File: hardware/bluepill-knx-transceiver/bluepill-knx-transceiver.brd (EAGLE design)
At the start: 37.6 x 38 mm, 22 parts, among them T1 BC856, T2 IRLL110

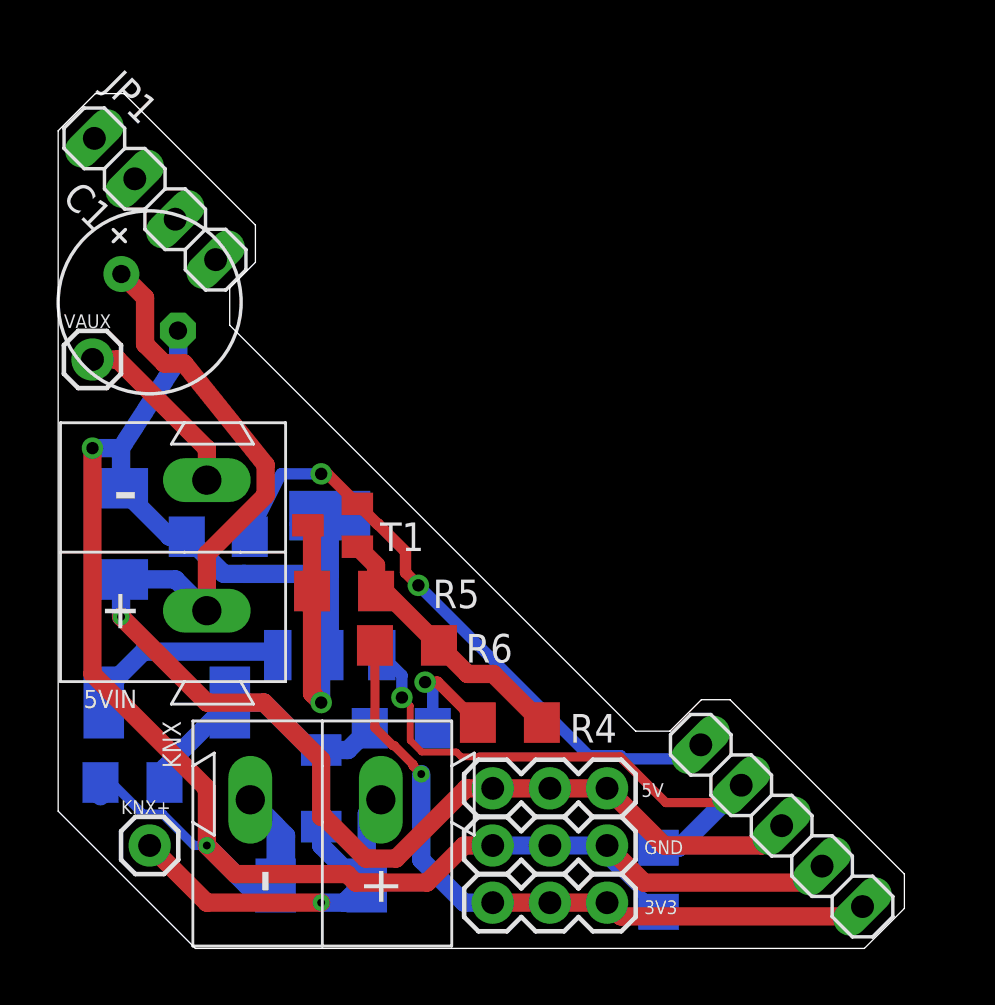
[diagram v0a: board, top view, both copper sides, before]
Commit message: transceiver board GND fills
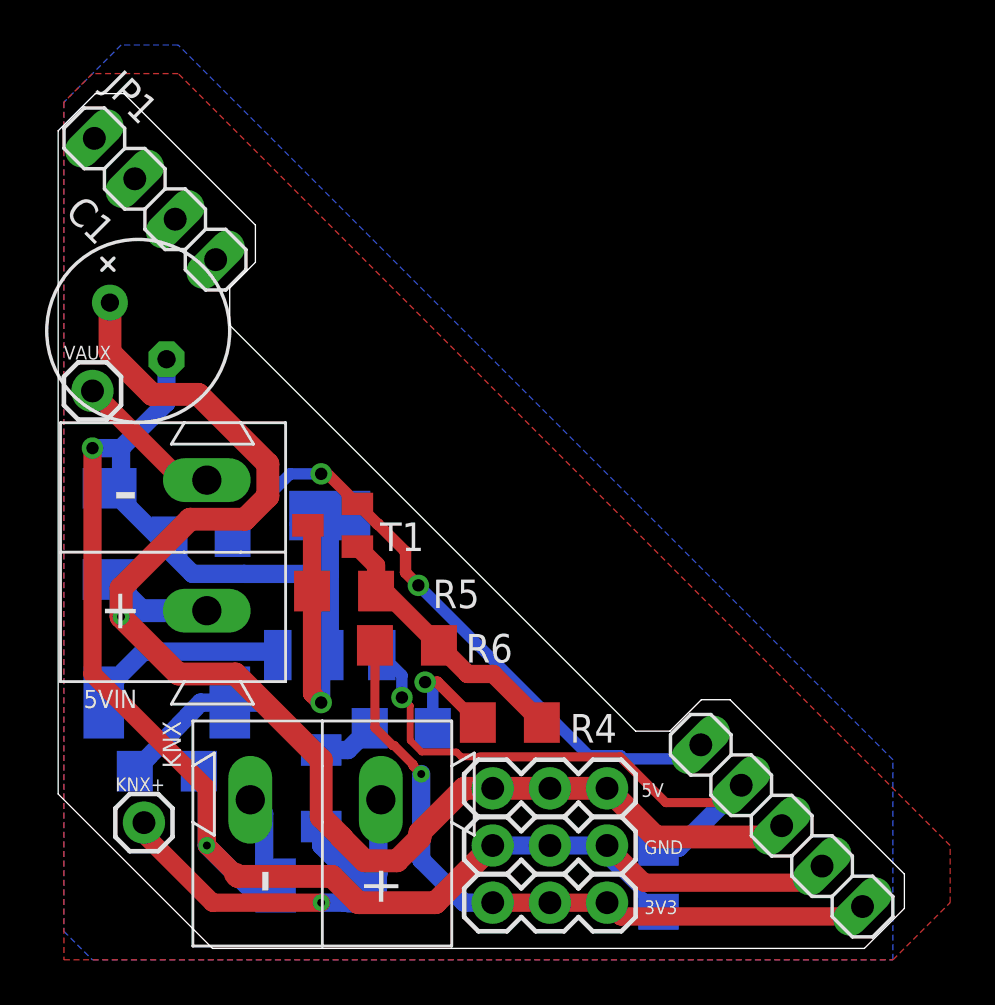
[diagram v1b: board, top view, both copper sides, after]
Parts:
- moved R3 1.61 mm to (60.5, 27.4), turned to 0 degrees
- moved VAUX 1.40 mm to (57.1, 44.3)
- moved C1 1.37 mm to (59.2, 47.0)
- moved KNX+ 1.05 mm to (59.4, 25.1)
- moved C3 0.76 mm to (62.0, 37.8)
- moved D1 0.51 mm to (57.9, 38.0)
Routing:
- net GND: track 111.8 -> 104.2 mm
- net 5V: track 63.0 -> 66.9 mm
- net VAUX: track 8.12 -> 6.72 mm
- net EIB+: track 19.1 -> 19.9 mm
- net KNX+D: track 12.2 -> 13.0 mm
- added copper zone on layer 1, net GND
- added copper zone on layer 16, net GND
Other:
- outline, holes or cut-outs redrawn

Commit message: prepared for DCDC
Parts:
- added CSEL: (no value), jumper:SJ_2
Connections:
- new net N$3: C1.+, CSEL.2
- net 5V: now also CSEL.1; no longer C1.+
- net VAUX: now also CSEL.3
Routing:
- net N$3: track 0.00 -> 8.71 mm
- net GND: track 104.2 -> 111.9 mm
- net 5V: track 66.9 -> 60.5 mm, vias 1 -> 2
- net VAUX: track 6.72 -> 7.70 mm
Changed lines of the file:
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@@
 <layer number="27" name="tValues" color="7" fill="1" visible="no" active="yes"/>
 <layer number="28" name="bValues" color="7" fill="1" visible="no" active="yes"/>
-<layer number="29" name="tStop" color="7" fill="3" visible="no" active="yes"/>
+<layer number="29" name="tStop" color="7" fill="3" visible="yes" active="yes"/>
 <layer number="30" name="bStop" color="7" fill="6" visible="no" active="yes"/>
 <layer number="31" name="tCream" color="7" fill="4" visible="no" active="yes"/>
@@
 <wire x1="58.547" y1="57.531" x2="57.277" y2="57.531" width="0" layer="20"/>
 <wire x1="55.626" y1="55.88" x2="57.277" y2="57.531" width="0" layer="20"/>
+<rectangle x1="59.69" y1="36.576" x2="65.151" y2="37.719" layer="29"/>
 </plain>
 <attributes>
@@
 <attribute name="VALUE" x="73.66" y="19.558" size="0.6096" layer="27" font="vector" ratio="20"/>
 </element>
+<element name="CSEL" library="jumper" library_urn="urn:adsk.eagle:library:252" package="SJ_2" package3d_urn="urn:adsk.eagle:package:15474/1" value="" x="62.738" y="43.053" rot="MR0"/>
 </elements>
 <signals>
@@
 <wire x1="64.777" y1="22.86" x2="65.285" y2="22.352" width="0.8128" layer="16"/>
 <wire x1="66.718" y1="38.354" x2="66.904" y2="38.168" width="0.8128" layer="1"/>
-<wire x1="66.904" y1="38.168" x2="66.904" y2="35.433" width="0.8128" layer="1"/>
+<wire x1="66.904" y1="38.168" x2="66.904" y2="36.83" width="0.8128" layer="1"/>
+<wire x1="66.904" y1="36.83" x2="66.904" y2="35.433" width="0.8128" layer="1"/>
 <wire x1="66.904" y1="35.433" x2="66.904" y2="30.886" width="0.8128" layer="1"/>
 <wire x1="66.904" y1="30.886" x2="67.31" y2="30.48" width="0.8128" layer="1"/>
@@
 <wire x1="63.88240625" y1="36.1964" x2="63.88380625" y2="36.195" width="0.8128" layer="16"/>
 <wire x1="63.88380625" y1="36.195" x2="67.691" y2="36.195" width="0.8128" layer="16"/>
-<wire x1="60.439234375" y1="43.802234375" x2="60.439234375" y2="45.7327625" width="0.8128" layer="16"/>
-<wire x1="58.42" y1="41.783" x2="60.439234375" y2="43.802234375" width="0.8128" layer="16"/>
 <wire x1="63.88240625" y1="36.1964" x2="61.5936" y2="36.1964" width="0.8128" layer="16"/>
 <wire x1="60.576" y1="37.214" x2="60.576" y2="37.846" width="0.8128" layer="16"/>
@@
 <wire x1="72.39" y1="21.59" x2="74.93" y2="24.13" width="1.016" layer="1"/>
 <wire x1="68.96236875" y1="21.59" x2="72.39" y2="21.59" width="1.016" layer="1"/>
+<wire x1="57.15" y1="41.783" x2="60.439234375" y2="45.072234375" width="1.016" layer="1"/>
+<wire x1="60.439234375" y1="45.072234375" x2="60.439234375" y2="45.7327625" width="1.016" layer="1"/>
+<wire x1="66.904" y1="36.83" x2="66.523" y2="37.211" width="1.016" layer="1"/>
+<wire x1="66.523" y1="37.211" x2="59.944" y2="37.211" width="1.016" layer="1"/>
 </signal>
 <signal name="PB8_KNX_RX">
@@
 <wire x1="70.89675625" y1="31.69384375" x2="70.0024" y2="32.5882" width="0.508" layer="16"/>
 <wire x1="74.3513375" y1="28.067" x2="80.5886625" y2="28.067" width="0.4064" layer="1"/>
-<wire x1="71.7776625" y1="28.2831" x2="73.3169" y2="28.2831" width="0.3048" layer="1"/>
 <wire x1="71.26506875" y1="30.33493125" x2="70.89675625" y2="30.70324375" width="0.3048" layer="1"/>
-<wire x1="71.7776625" y1="28.2831" x2="71.26506875" y2="28.79569375" width="0.3048" layer="1"/>
 <wire x1="71.26506875" y1="28.79569375" x2="71.26506875" y2="30.33493125" width="0.3048" layer="1"/>
-<wire x1="73.3169" y1="28.2831" x2="73.533" y2="28.067" width="0.3048" layer="1"/>
-<wire x1="73.533" y1="28.067" x2="74.3513375" y2="28.067" width="0.3048" layer="1"/>
+<wire x1="73.533" y1="28.067" x2="73.66" y2="28.067" width="0.3048" layer="1"/>
 <contactref element="JP1" pad="17"/>
+<wire x1="73.66" y1="28.067" x2="74.3513375" y2="28.067" width="0.3048" layer="1"/>
 <wire x1="85.197665625" y1="26.035" x2="85.96933125" y2="26.806665625" width="0.4064" layer="1"/>
 <wire x1="80.5886625" y1="28.067" x2="82.6206625" y2="26.035" width="0.4064" layer="1"/>
@@
 <wire x1="82.296" y1="24.028" x2="83.190665625" y2="24.028" width="0.8128" layer="16"/>
 <wire x1="83.190665625" y1="24.028" x2="85.96933125" y2="26.806665625" width="0.8128" layer="16"/>
+<wire x1="72.10259375" y1="28.067" x2="72.07999375" y2="28.0896" width="0.3048" layer="1"/>
+<wire x1="72.07999375" y1="28.0896" x2="71.9711625" y2="28.0896" width="0.3048" layer="1"/>
+<wire x1="73.533" y1="28.067" x2="72.10259375" y2="28.067" width="0.3048" layer="1"/>
+<wire x1="71.9711625" y1="28.0896" x2="71.26506875" y2="28.79569375" width="0.3048" layer="1"/>
 </signal>
 <signal name="VAUX">
 <contactref element="5VIN" pad="2-"/>
 <contactref element="VAUX" pad="1"/>
-<wire x1="57.15" y1="44.323" x2="61.112" y2="40.361" width="0.8128" layer="1"/>
-<wire x1="61.112" y1="40.361" x2="62.23" y2="40.361" width="0.8128" layer="1"/>
+<contactref element="CSEL" pad="3"/>
+<wire x1="61.214" y1="43.053" x2="61.087" y2="43.18" width="1.016" layer="16"/>
+<wire x1="58.293" y1="43.18" x2="57.15" y2="44.323" width="1.016" layer="16"/>
+<wire x1="61.087" y1="43.18" x2="58.293" y2="43.18" width="1.016" layer="16"/>
+<wire x1="61.214" y1="43.053" x2="61.214" y2="41.377" width="1.016" layer="16"/>
+<wire x1="61.214" y1="41.377" x2="62.23" y2="40.361" width="1.016" layer="16"/>
 </signal>
 <signal name="5V">
 <contactref element="5VIN" pad="1+"/>
 <contactref element="D1" pad="C"/>
-<contactref element="C1" pad="+"/>
 <contactref element="5V" pad="2"/>
 <contactref element="5V" pad="3"/>
@@
 <wire x1="57.912" y1="35.948" x2="59.299" y2="34.561" width="1.016" layer="16"/>
 <wire x1="59.299" y1="34.561" x2="62.23" y2="34.561" width="1.016" layer="16"/>
-<wire x1="58.42" y1="34.29" x2="58.42" y2="35.56" width="1.016" layer="1"/>
-<wire x1="61.484" y1="38.624" x2="63.92449375" y2="38.624" width="1.016" layer="1"/>
 <wire x1="63.92449375" y1="38.624" x2="64.942" y2="39.64150625" width="1.016" layer="1"/>
-<wire x1="58.42" y1="35.56" x2="61.484" y2="38.624" width="1.016" layer="1"/>
-<wire x1="64.942" y1="41.08049375" x2="61.8518375" y2="44.17065625" width="1.016" layer="1"/>
-<wire x1="61.8518375" y1="44.17065625" x2="59.7921875" y2="44.17065625" width="1.016" layer="1"/>
-<wire x1="59.7921875" y1="44.17065625" x2="57.9247625" y2="46.03808125" width="1.016" layer="1"/>
-<wire x1="64.942" y1="39.64150625" x2="64.942" y2="41.08049375" width="1.016" layer="1"/>
-<wire x1="57.9247625" y1="46.03808125" x2="57.9247625" y2="48.247234375" width="1.016" layer="1"/>
+<wire x1="63.92449375" y1="38.624" x2="59.198" y2="38.624" width="1.016" layer="1"/>
+<wire x1="59.198" y1="38.624" x2="58.42" y2="37.846" width="1.016" layer="1"/>
+<wire x1="58.42" y1="37.846" x2="58.42" y2="34.29" width="1.016" layer="1"/>
+<contactref element="CSEL" pad="1"/>
+<wire x1="64.942" y1="39.64150625" x2="64.942" y2="40.812" width="1.016" layer="1"/>
+<wire x1="64.942" y1="40.812" x2="66.04" y2="41.91" width="1.016" layer="1"/>
+<via x="66.04" y="41.91" extent="1-16" drill="0.35"/>
+<wire x1="66.04" y1="41.91" x2="64.897" y2="43.053" width="1.016" layer="16"/>
+<wire x1="64.897" y1="43.053" x2="64.262" y2="43.053" width="1.016" layer="16"/>
+</signal>
+<signal name="N$3">
+<contactref element="C1" pad="+"/>
+<contactref element="CSEL" pad="2"/>
+<wire x1="57.9247625" y1="47.8662375" x2="57.9247625" y2="48.247234375" width="1.016" layer="16"/>
+<wire x1="62.738" y1="43.053" x2="62.5602" y2="43.2308" width="1.016" layer="16"/>
+<wire x1="58.496134375" y1="47.294865625" x2="57.9247625" y2="47.8662375" width="1.016" layer="16"/>
+<wire x1="61.086284375" y1="47.294865625" x2="58.496134375" y2="47.294865625" width="1.016" layer="16"/>
+<wire x1="62.5602" y1="43.2308" x2="62.5602" y2="45.82095" width="1.016" layer="16"/>
+<wire x1="62.5602" y1="45.82095" x2="61.086284375" y2="47.294865625" width="1.016" layer="16"/>
+</signal>
+<signal name="N$4">
+<via x="60.071" y="36.068" extent="1-16" drill="0.35"/>
+</signal>
+<signal name="N$9">
+<via x="65.151" y="35.052" extent="1-16" drill="0.35"/>
 </signal>
 </signals>
